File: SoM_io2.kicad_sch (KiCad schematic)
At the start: 8 parts, among them J1 Hermaphroditic_Molex_203456-0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, Y2 Oscillator_156.25MHz_SG3225EEN

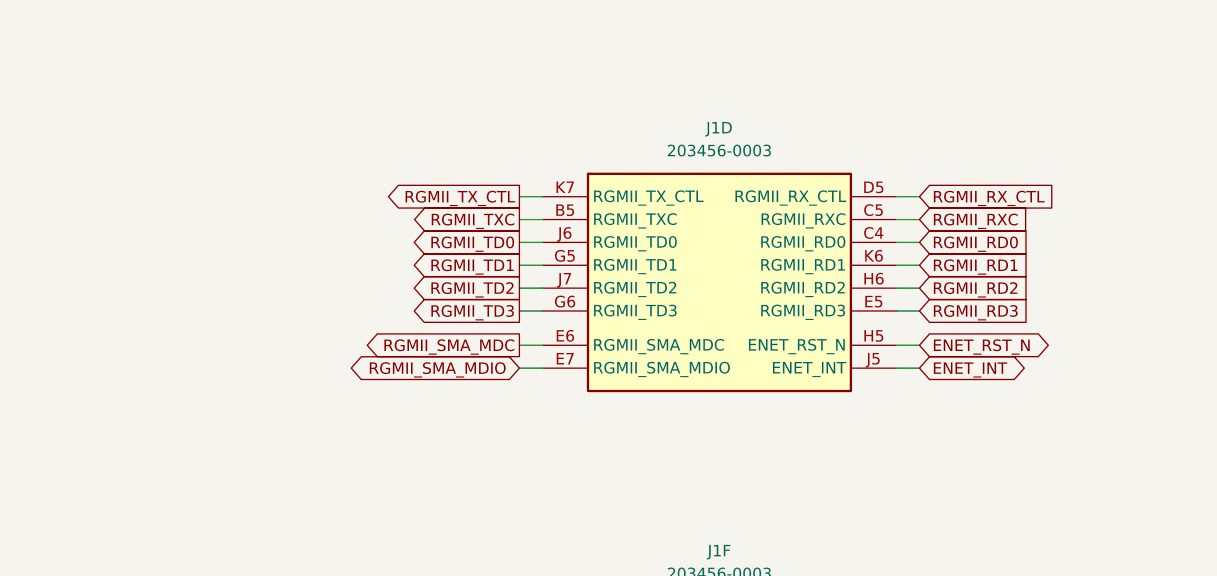
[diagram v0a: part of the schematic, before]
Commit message: [#82057] Route out RGMII from SoM
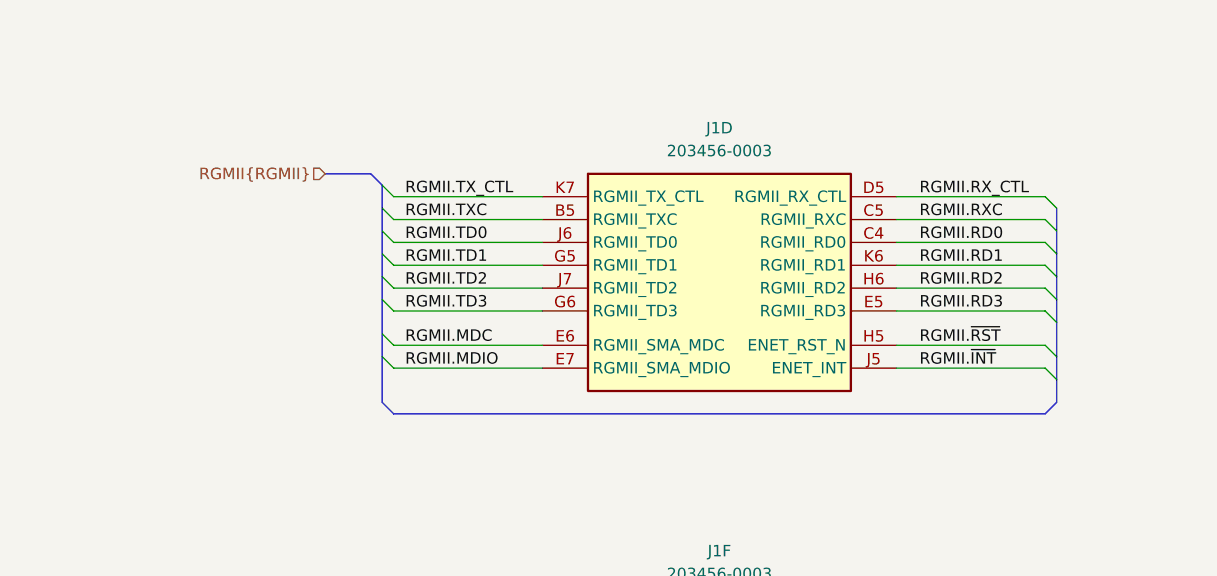
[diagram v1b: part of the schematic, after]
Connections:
- net ENET_INT renamed RGMII.~{INT}
- net ENET_RST_N renamed RGMII.~{RST}
- net RGMII_RD0 renamed RGMII.RD0
- net RGMII_RD1 renamed RGMII.RD1
- net RGMII_RD2 renamed RGMII.RD2
- net RGMII_RD3 renamed RGMII.RD3
- net RGMII_RXC renamed RGMII.RXC
- net RGMII_RX_CTL renamed RGMII.RX_CTL
- net RGMII_SMA_MDC renamed RGMII.MDC
- net RGMII_SMA_MDIO renamed RGMII.MDIO
- net RGMII_TD0 renamed RGMII.TD0
- net RGMII_TD1 renamed RGMII.TD1
- net RGMII_TD2 renamed RGMII.TD2
- net RGMII_TD3 renamed RGMII.TD3
- net RGMII_TXC renamed RGMII.TXC
- net RGMII_TX_CTL renamed RGMII.TX_CTL

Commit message: [#82757] Rename project to jetson-agx-thor-baseboard
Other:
- title: Jetson Orin AGX Baseboard -> Jetson AGX Thor Baseboard
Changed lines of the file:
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@@
 	(paper "A3")
 	(title_block
-		(title "Jetson Orin AGX Baseboard")
+		(title "Jetson AGX Thor Baseboard")
 		(date "2025-08-11")
 		(rev "1.0.0")

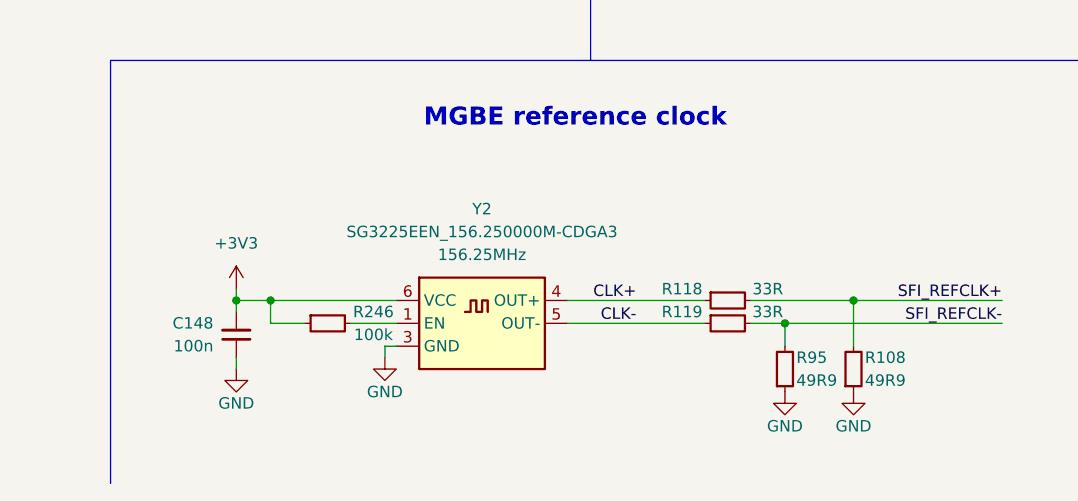
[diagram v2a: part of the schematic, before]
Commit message: [#82757] Cleanup: reorganise page numbers and fix annotations
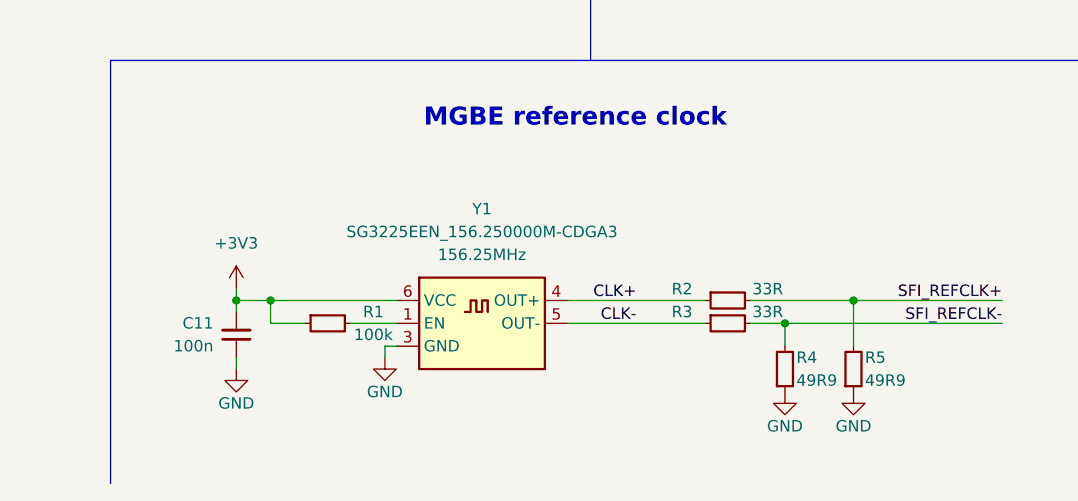
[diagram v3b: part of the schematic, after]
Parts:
- renumbered C148 to C11, R246 to R1, R118 to R2, R119 to R3, R95 to R4, R108 to R5, Y2 to Y1
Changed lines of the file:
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@@
 		(on_board yes)
 		(dnp no)
-		(property "Reference" "R119"
+		(property "Reference" "R3"
 			(at 255.27 265.43 0)
 			(effects
@@
 			(project "jetson-orin-agx-baseboard"
 				(path "/f569b0be-0afd-48b7-93ee-28582a4c645c/656db8bb-c788-4c93-9592-ce18fa1a48a2"
-					(reference "R119")
+					(reference "R3")
 					(unit 1)
 				)
@@
 		(on_board yes)
 		(dnp no)
-		(property "Reference" "R95"
+		(property "Reference" "R4"
 			(at 267.97 270.51 90)
 			(effects
@@
 			(project "jetson-orin-agx-baseboard"
 				(path "/f569b0be-0afd-48b7-93ee-28582a4c645c/656db8bb-c788-4c93-9592-ce18fa1a48a2"
-					(reference "R95")
+					(reference "R4")
 					(unit 1)
 				)
@@
 		(on_board yes)
 		(dnp no)
-		(property "Reference" "#PWR0331"
+		(property "Reference" "#PWR028"
 			(at 222.25 276.86 0)
 			(effects
@@
 			(project "jetson-orin-agx-baseboard"
 				(path "/f569b0be-0afd-48b7-93ee-28582a4c645c/656db8bb-c788-4c93-9592-ce18fa1a48a2"
-					(reference "#PWR0331")
+					(reference "#PWR028")
 					(unit 1)
 				)
@@
 		(on_board yes)
 		(dnp no)
-		(property "Reference" "R108"
+		(property "Reference" "R5"
 			(at 275.59 270.51 90)
 			(effects
@@
 			(project "jetson-orin-agx-baseboard"
 				(path "/f569b0be-0afd-48b7-93ee-28582a4c645c/656db8bb-c788-4c93-9592-ce18fa1a48a2"
-					(reference "R108")
+					(reference "R5")
 					(unit 1)
 				)
@@
 		(dnp no)
 		(fields_autoplaced yes)
-		(property "Reference" "#PWR0327"
+		(property "Reference" "#PWR026"
 			(at 220.98 262.89 0)
 			(effects
@@
 			(project "jetson-orin-agx-baseboard"
 				(path "/f569b0be-0afd-48b7-93ee-28582a4c645c/656db8bb-c788-4c93-9592-ce18fa1a48a2"
-					(reference "#PWR0327")
+					(reference "#PWR026")
 					(unit 1)
 				)
@@
 		(on_board yes)
 		(dnp no)
-		(property "Reference" "#PWR0144"
+		(property "Reference" "#PWR030"
 			(at 283.21 276.86 0)
 			(effects
@@
 			(project "jetson-orin-agx-baseboard"
 				(path "/f569b0be-0afd-48b7-93ee-28582a4c645c/656db8bb-c788-4c93-9592-ce18fa1a48a2"
-					(reference "#PWR0144")
+					(reference "#PWR030")
 					(unit 1)
 				)
@@
 		(on_board yes)
 		(dnp no)
-		(property "Reference" "#PWR0143"
+		(property "Reference" "#PWR029"
 			(at 275.59 276.86 0)
 			(effects
@@
 			(project "jetson-orin-agx-baseboard"
 				(path "/f569b0be-0afd-48b7-93ee-28582a4c645c/656db8bb-c788-4c93-9592-ce18fa1a48a2"
-					(reference "#PWR0143")
+					(reference "#PWR029")
 					(unit 1)
 				)
@@
 		(on_board yes)
 		(dnp no)
-		(property "Reference" "R118"
+		(property "Reference" "R2"
 			(at 255.27 262.89 0)
 			(effects
@@
 			(project "jetson-orin-agx-baseboard"
 				(path "/f569b0be-0afd-48b7-93ee-28582a4c645c/656db8bb-c788-4c93-9592-ce18fa1a48a2"
-					(reference "R118")
+					(reference "R2")
 					(unit 1)
 				)
@@
 		(on_board yes)
 		(dnp no)
-		(property "Reference" "R246"
+		(property "Reference" "R1"
 			(at 220.98 265.43 0)
 			(effects
@@
 			(project "jetson-orin-agx-baseboard"
 				(path "/f569b0be-0afd-48b7-93ee-28582a4c645c/656db8bb-c788-4c93-9592-ce18fa1a48a2"
-					(reference "R246")
+					(reference "R1")
 					(unit 1)
 				)
@@
 		(dnp no)
 		(fields_autoplaced yes)
-		(property "Reference" "C148"
+		(property "Reference" "C11"
 			(at 203.2 266.6935 90)
 			(effects
@@
 			(project "jetson-orin-agx-baseboard"
 				(path "/f569b0be-0afd-48b7-93ee-28582a4c645c/656db8bb-c788-4c93-9592-ce18fa1a48a2"
-					(reference "C148")
+					(reference "C11")
 					(unit 1)
 				)
@@
 		(dnp no)
 		(fields_autoplaced yes)
-		(property "Reference" "Y2"
+		(property "Reference" "Y1"
 			(at 233.045 254 0)
 			(effects
@@
 			(project "jetson-orin-agx-baseboard"
 				(path "/f569b0be-0afd-48b7-93ee-28582a4c645c/656db8bb-c788-4c93-9592-ce18fa1a48a2"
-					(reference "Y2")
+					(reference "Y1")
 					(unit 1)
 				)
@@
 		(on_board yes)
 		(dnp no)
-		(property "Reference" "#PWR0328"
+		(property "Reference" "#PWR027"
 			(at 205.74 278.13 0)
 			(effects
@@
 			(project "jetson-orin-agx-baseboard"
 				(path "/f569b0be-0afd-48b7-93ee-28582a4c645c/656db8bb-c788-4c93-9592-ce18fa1a48a2"
-					(reference "#PWR0328")
+					(reference "#PWR027")
 					(unit 1)
 				)
